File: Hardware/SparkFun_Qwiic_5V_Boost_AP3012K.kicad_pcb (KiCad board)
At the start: 2 copper layers, 25.4 x 25.4 mm, 65 parts, among them J1 Qwiic_RA, J2 Qwiic_RA, J3 Conn_01x06, Q1 BSS138, Q2 BSS138, U5 AP3012

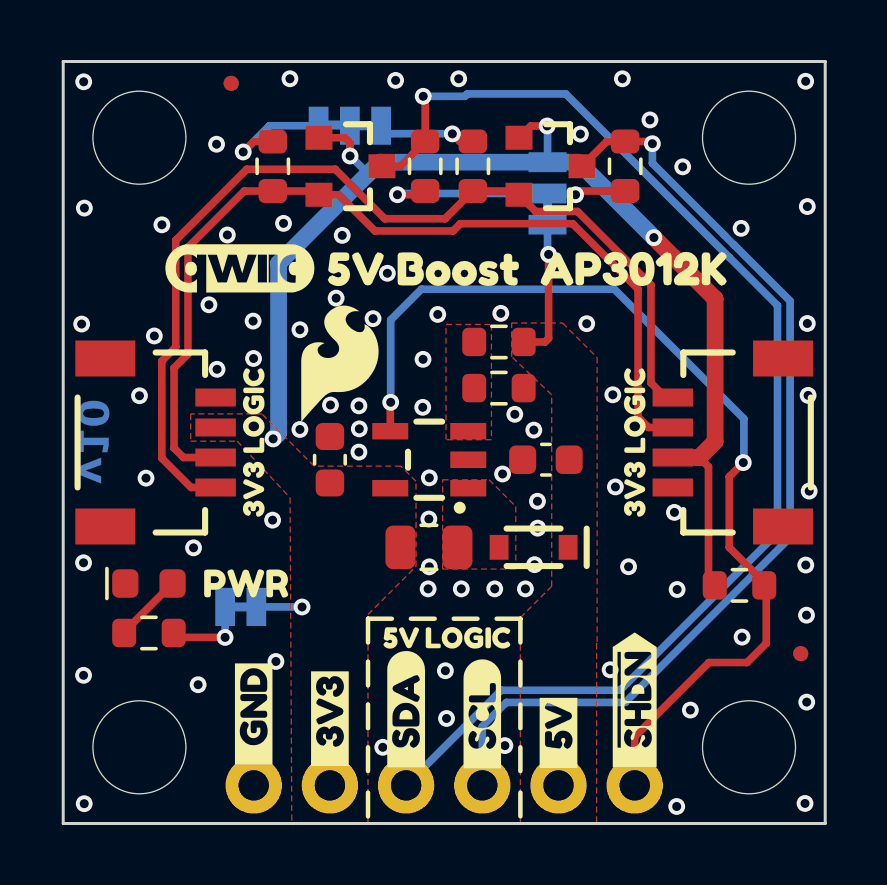
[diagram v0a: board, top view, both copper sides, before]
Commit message: I2C HV pullup jumper
-added pullup jumper for I2C HV
-Updated D2 to latest footprint
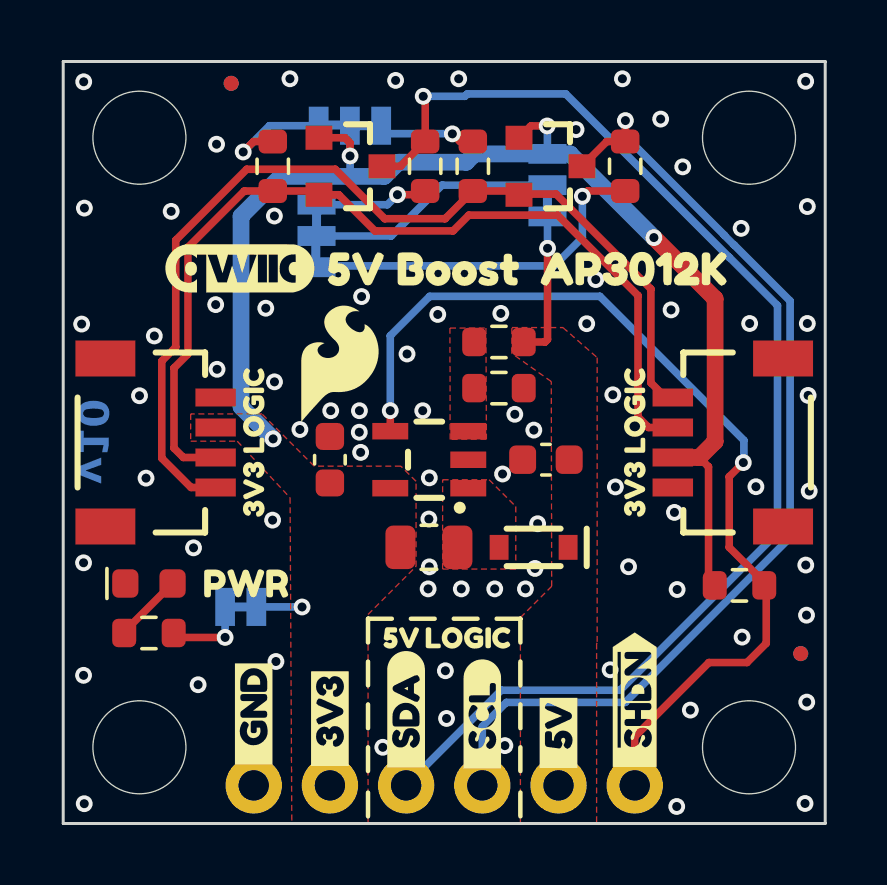
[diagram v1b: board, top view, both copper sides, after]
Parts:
- added JP4: I2C HV, SparkFun-Jumper:Jumper_3_NC-2_Trace, B.Cu at (131.7, 91.2)
- added kibuzzard-67C0A4F9: G***, kibuzzard-67C0A4F9, B.Cu at (128.5, 91.4)
- moved JP3 0.28 mm to (139.4, 89.5)
- moved kibuzzard-67A51B3F 0.26 mm to (141.9, 88.5)
- moved kibuzzard-67A51B57 0.26 mm to (141.6, 90.6)
- moved kibuzzard-67A51B2D 0.24 mm to (136.9, 89.6)
- moved kibuzzard-67AB7F1B 0.24 mm to (137.8, 89.5)
- moved kibuzzard-67AB7F2D 0.24 mm to (136.0, 89.6)
- moved kibuzzard-67A51507 0.06 mm to (136.0, 99.9)
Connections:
- L1 pad 2: Net-(U5-SW) -> Net-(D2-A)
- R7 pad 1: VCC -> Net-(JP4-A)
- R8 pad 1: VCC -> Net-(JP4-C)
- U5 pad 1: Net-(U5-SW) -> Net-(D2-A)
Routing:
- net Net-(JP4-C): track 0.00 -> 12.1 mm, vias 0 -> 1
- net Net-(JP4-A): track 0.00 -> 3.81 mm, vias 0 -> 1
- net 3.3V: track 41.7 -> 44.1 mm
- net ~{SHDN}: track 33.2 -> 32.3 mm
- net HV_SCL: track 32.6 -> 33.5 mm
- net VCC: track 8.65 -> 8.40 mm, vias 2 -> 0
- net GND: vias 79 -> 77
- added copper zone on F.Cu, net Net-(D2-A)
- removed copper zone on F.Cu, net Net-(U5-SW)

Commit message: final feedback
-BRD - turned on all layers to visible
-SCH - changed note about max current to 100mA
-nudged SDA trace to remove a bump
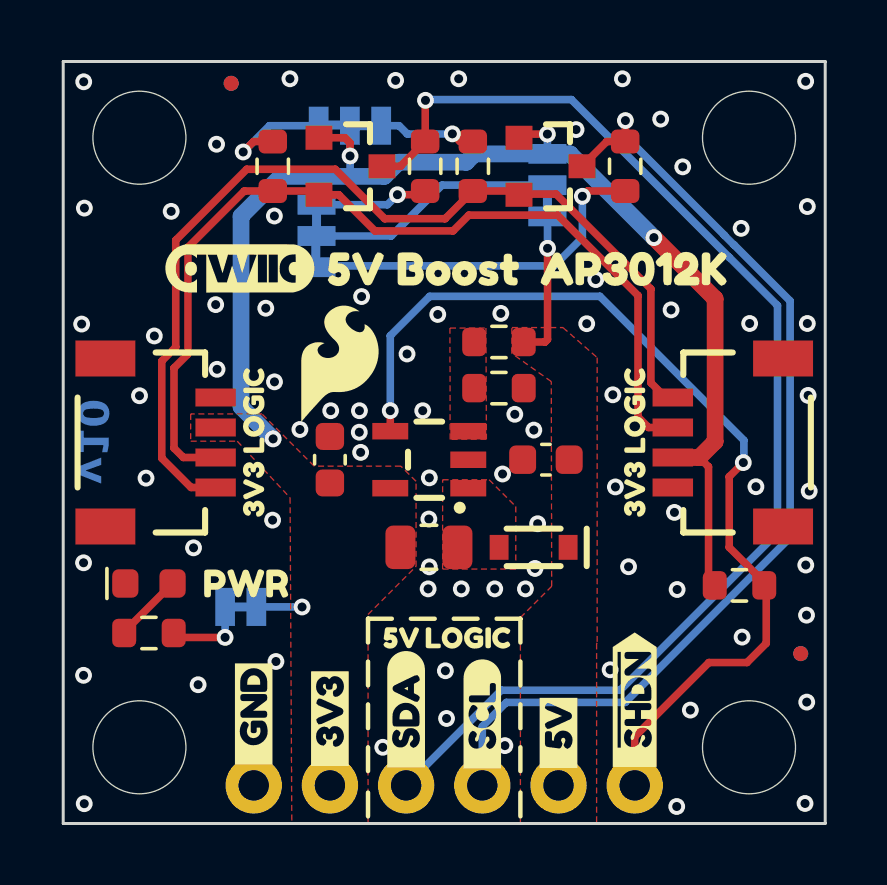
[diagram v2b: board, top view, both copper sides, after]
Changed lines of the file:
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@@
 		(tags "SparkFun")
 		(property "Reference" "D2"
-			(at 0 -0.762 360)
+			(at 0 -0.762 0)
 			(layer "F.Fab")
 			(effects
@@
 		)
 		(property "Value" "PMEG4005EJ"
-			(at 0 0.762 360)
+			(at 0 0.762 0)
 			(layer "F.Fab")
 			(effects
@@
 				(font
 					(size 0.001 0.001)
+					(thickness 0.15)
 				)
 				(justify mirror)
@@
 				(font
 					(size 0.001 0.001)
+					(thickness 0.15)
 				)
 				(justify mirror)
@@
 	)
 	(segment
-		(start 138.853 87.554)
-		(end 138.4585 87.9485)
-		(width 0.254)
-		(layer "F.Cu")
-		(net 1)
-	)
-	(segment
 		(start 144.996 93.316)
 		(end 144.996 98.076)
@@
 	)
 	(segment
+		(start 138.4585 87.9485)
+		(end 138.581 87.826)
+		(width 0.254)
+		(layer "F.Cu")
+		(net 1)
+	)
+	(segment
 		(start 143.721 98.606)
 		(end 144.466 98.606)
@@
 	)
 	(segment
-		(start 139.398 87.554)
-		(end 138.853 87.554)
+		(start 145.05 102.836)
+		(end 144.776 102.562)
 		(width 0.254)
 		(layer "F.Cu")
@@
 	)
 	(segment
-		(start 145.05 102.836)
-		(end 144.776 102.562)
+		(start 138.581 87.826)
+		(end 139.406 87.826)
 		(width 0.254)
 		(layer "F.Cu")
@@
 	)
 	(via
-		(at 139.398 87.554)
+		(at 139.406 87.826)
 		(size 0.56)
 		(drill 0.3)
@@
 	(segment
 		(start 139.406 88.4866)
-		(end 140.165238 88.4866)
-		(width 0.5588)
+		(end 139.406 87.826)
+		(width 0.254)
 		(layer "B.Cu")
 		(net 1)
@@
 	(segment
 		(start 139.406 88.4866)
-		(end 139.406 87.562)
-		(width 0.254)
+		(end 140.165238 88.4866)
+		(width 0.5588)
 		(layer "B.Cu")
 		(net 1)
@@
 	)
 	(segment
-		(start 139.406 87.562)
-		(end 139.398 87.554)
-		(width 0.254)
-		(layer "B.Cu")
-		(net 1)
-	)
-	(segment
 		(start 132.828 88.556)
 		(end 132.828 89.231)
@@
 	)
 	(segment
-		(start 139.411 87.567)
-		(end 139.398 87.554)
-		(width 0.254)
-		(layer "B.Cu")
-		(net 1)
-	)
-	(segment
 		(start 129.194 90.561)
 		(end 129.194 96.916)
@@
 	)
 	(segment
-		(start 136.236958 87.818503)
-		(end 136.229455 87.811)
+		(start 134.736 87.822)
+		(end 134.461 87.547)
 		(width 0.254)
 		(layer "B.Cu")
@@
 	)
 	(segment
-		(start 136.229455 87.811)
-		(end 134.1284 87.811)
+		(start 134.461 87.547)
+		(end 133.8644 87.547)
 		(width 0.254)
 		(layer "B.Cu")
@@
 	)
 	(segment
-		(start 134.1284 87.811)
-		(end 133.8644 87.547)
+		(start 136.233461 87.822)
+		(end 134.736 87.822)
+		(width 0.254)
+		(layer "B.Cu")
+		(net 12)
+	)
+	(segment
+		(start 136.236958 87.818503)
+		(end 136.233461 87.822)
 		(width 0.254)
 		(layer "B.Cu")
@@
 	)
 	(segment
-		(start 135.331 86.631)
-		(end 135.266 86.566)
+		(start 133.891 88.8985)
+		(end 134.506 88.8985)
 		(width 0.254)
 		(layer "F.Cu")
@@
 	)
 	(segment
-		(start 135.331 88.0735)
-		(end 135.331 86.631)
+		(start 134.506 88.8985)
+		(end 135.331 88.0735)
 		(width 0.254)
 		(layer "F.Cu")
@@
 	)
 	(segment
-		(start 133.891 88.8985)
-		(end 134.506 88.8985)
+		(start 135.331 86.711)
+		(end 135.331 88.0735)
 		(width 0.254)
 		(layer "F.Cu")
@@
 	)
 	(segment
-		(start 134.506 88.8985)
-		(end 135.331 88.0735)
+		(start 135.342 86.7)
+		(end 135.331 86.711)
 		(width 0.254)
 		(layer "F.Cu")
@@
 	)
 	(via
-		(at 135.266 86.566)
+		(at 135.342 86.7)
 		(size 0.56)
 		(drill 0.3)
@@
 	)
 	(segment
-		(start 141.831664 106.3636)
-		(end 137.8684 106.3636)
+		(start 135.367 86.675)
+		(end 140.205152 86.675)
 		(width 0.254)
 		(layer "B.Cu")
@@
 	)
 	(segment
-		(start 136.656112 86.566)
-		(end 136.736112 86.486)
+		(start 135.342 86.7)
+		(end 135.367 86.675)
 		(width 0.254)
 		(layer "B.Cu")
@@
 	)
 	(segment
-		(start 140.016152 86.486)
-		(end 145.463952 91.9338)
-		(width 0.254)
-		(layer "B.Cu")
-		(net 16)
-	)
-	(segment
-		(start 147.076 93.540736)
-		(end 147.076 101.119264)
+		(start 147.076 101.119264)
+		(end 141.831664 106.3636)
 		(width 0.254)
 		(layer "B.Cu")
@@
 	)
 	(segment
-		(start 136.736112 86.486)
-		(end 140.016152 86.486)
+		(start 141.831664 106.3636)
+		(end 137.8684 106.3636)
 		(width 0.254)
 		(layer "B.Cu")
@@
 	)
 	(segment
-		(start 135.266 86.566)
-		(end 136.656112 86.566)
+		(start 140.205152 86.675)
+		(end 145.463952 91.9338)
 		(width 0.254)
 		(layer "B.Cu")
@@
 	)
 	(segment
-		(start 147.076 101.119264)
-		(end 141.831664 106.3636)
+		(start 147.076 93.540736)
+		(end 147.076 101.119264)
 		(width 0.254)
 		(layer "B.Cu")
